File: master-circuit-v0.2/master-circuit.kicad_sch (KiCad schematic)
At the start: 128 parts, among them U6 20nF 5%, X2 24MHz

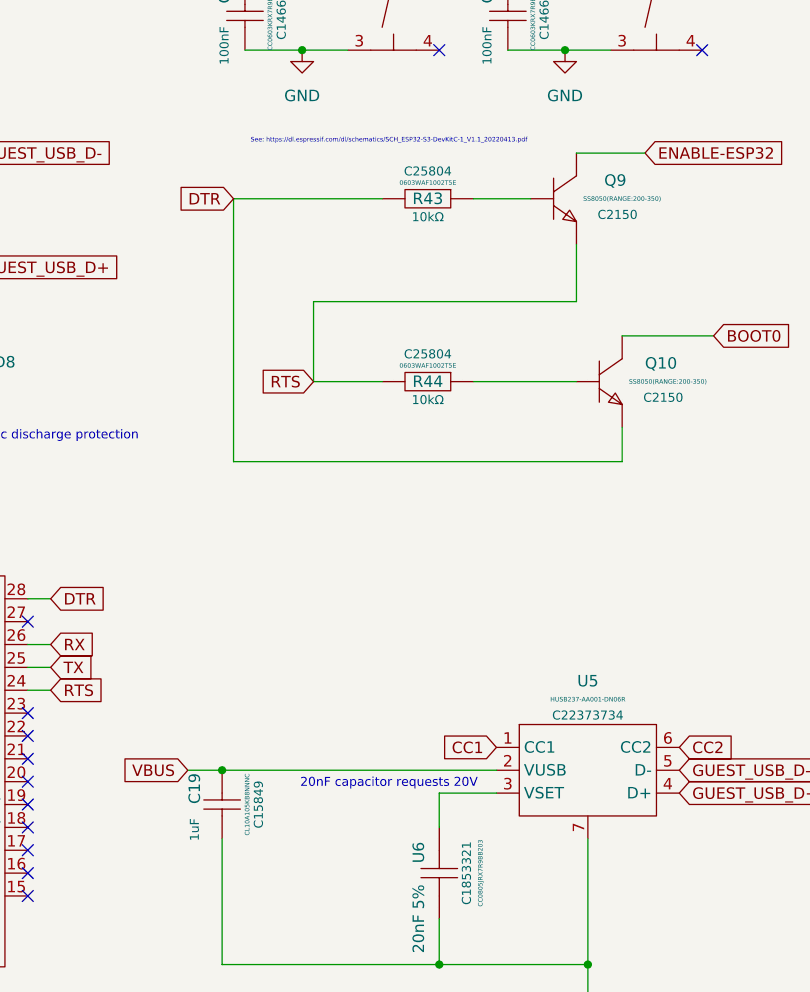
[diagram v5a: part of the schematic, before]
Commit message: Deal with most of the connection spider web, connector lines remaining.
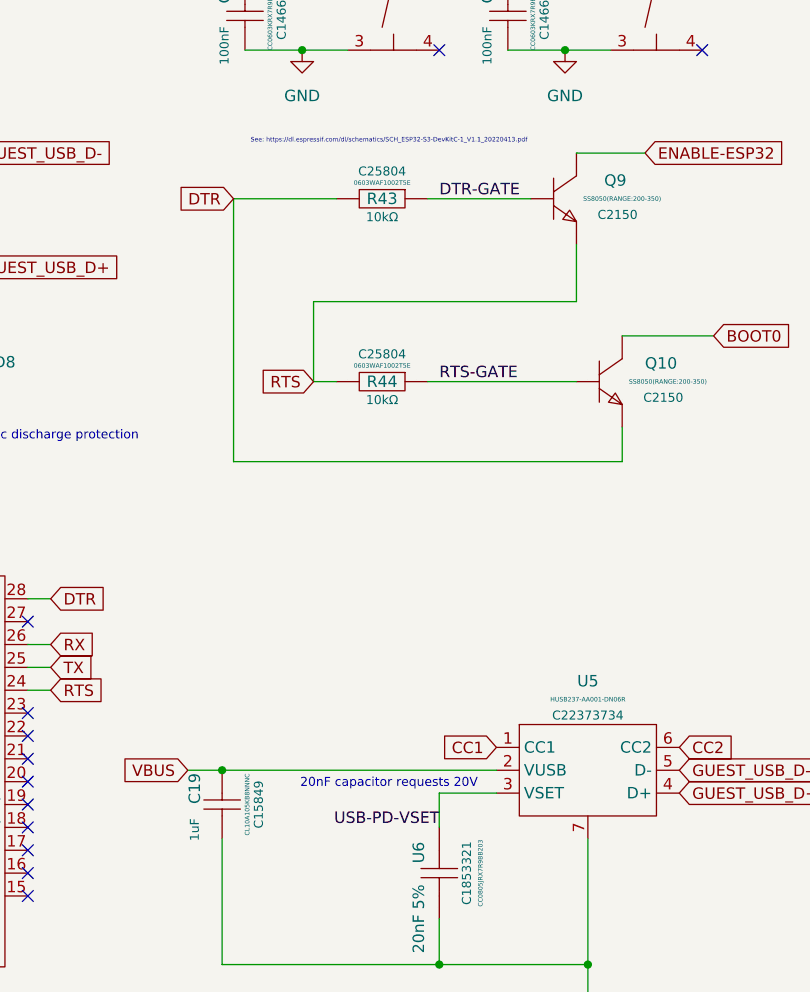
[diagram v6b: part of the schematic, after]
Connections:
- net USB-PD-VSET: now reaches U5.3 (VSET), U6.2
- net RTS-GATE: now reaches Q10.1 (B), R44.1
- net DTR-GATE: now reaches Q9.1 (B), R43.1
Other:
- moved on the sheet: R43, R44

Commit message: USB hub lines remaining.
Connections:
- net +Probe-1: now also U11.3 (IN±1); no longer U11.4 (IN+1)
- net +Probe-2: now also U11.7 (IN±2); no longer U11.6 (IN+2)
- net +Probe-4: now also U11.18 (IN±4); no longer U11.17 (IN+4)
- net +Probe-7: now also U16.14 (IN±3); no longer U16.15 (IN+3)
- net -Probe-1: now also U11.4 (IN+1); no longer U11.3 (IN±1)
- net -Probe-2: now also U11.6 (IN+2); no longer U11.7 (IN±2)
- net -Probe-4: now also U11.17 (IN+4); no longer U11.18 (IN±4)
- net -Probe-7: now also U16.15 (IN+3); no longer U16.14 (IN±3)
- net BATTERY_VOLTAGE: now also U1.39 (IO1); no longer U1.9 (IO16)
- net SERVO1_CURRENT: now also U1.15 (IO3); no longer U1.39 (IO1)
- net SERVO2_CURRENT: now also U1.12 (IO8); no longer U1.38 (IO2)
- net SERVO3_CURRENT: now also U1.9 (IO16); no longer U1.15 (IO3)
- net SERVO4_CURRENT: now also U1.8 (IO15); no longer U1.4 (IO4)
- net SERVO5_CURRENT: now also U1.4 (IO4); no longer U1.5 (IO5)
- net SERVO6_CURRENT: now also U1.7 (IO7); no longer U1.6 (IO6)
- net VBUS_VOLTAGE: now also U1.38 (IO2); no longer U1.8 (IO15)
- net SERVO7_CURRENT renamed VBUS_CURRENT
- net VBUS_CURRENT: now also U1.6 (IO6); no longer U1.7 (IO7)
- net VCC_CURRENT renamed BATTERY_CURRENT
- net BATTERY_CURRENT: now also U1.5 (IO5); no longer U1.12 (IO8)

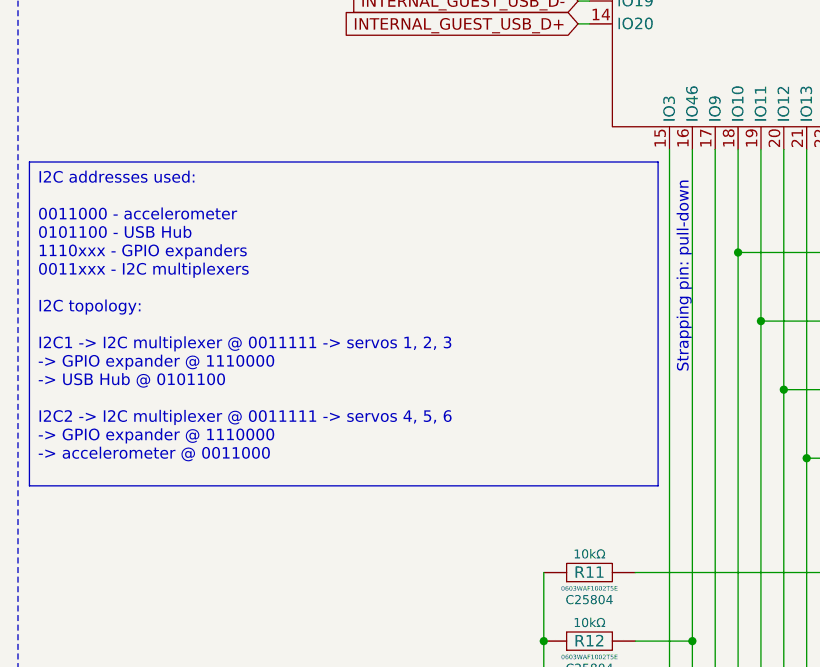
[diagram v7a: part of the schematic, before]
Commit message: Make schematic for the cable plug and extension circuit.
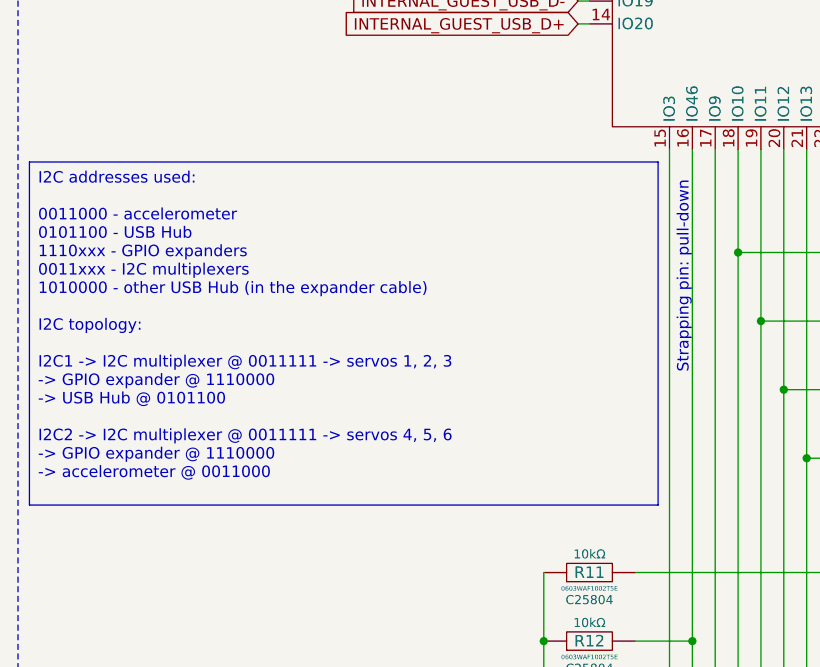
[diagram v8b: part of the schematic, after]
